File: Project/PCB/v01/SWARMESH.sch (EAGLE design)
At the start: 45 parts, among them IC1 4051N, M1 MOTOR10MM, M2 MOTOR10MM, Q1 TIP122, U1 ESP32DEVKITC, U3 L293D, U4 7805T

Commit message: added datasheets
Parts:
- removed C1: 10uF, adafruit:CPOL-USE10-20
- removed JBAT, JCHG: (no value), SparkFun-Connectors:M02-JST-2-PTH-NO_SILK
- removed LED1: TLLG4400, led:TLLG4400
- removed LED2: TLLR4400, led:TLLR4400
- removed LED3: TLLY4400, led:TLLY4400
- removed R1, R3: PHOTOCELLPTH, SparkFun-Sensors:PHOTOCELLPTH
- removed R10, R2, R4, R5, R6, R7: 1k, adafruit:R-US_0207/12
- removed R11, R8: 100, adafruit:R-US_0207/12
- removed R12, R9: 10k, adafruit:R-US_0207/12
- removed S1: (no value), SparkFun-Electromechanical:SWITCH-SPDTPTH2
- removed U$1, U$2: CNY70, cny70:CNY70
- removed U$3: PNA460XM, adafruit:PNA460XM
- removed U$4: PINHD-1X10, adafruit:PINHD-1X10
- added BAT+, BAT-, CHG1+, CHG1-, CHG2+, CHG2-: (no value), adafruit:PINHD-1X1-BIGPOGO
- added C5, C6: 10uF, adafruit:CPOL-USE2.5-7
- added JMUX: PINHD-1X10, adafruit:PINHD-1X10
- added RD1, RD2: 0, adafruit:R-US_0207/12
- added RS1, RS2: 150, adafruit:R-US_0207/12
- added S2: (no value), ArduinoNano LearningBot 4-21-18:SWITCH_320-938
- added T1, T2, T3, T4: (no value), SparkFun-Connectors:CONN_01SPRING-CONN
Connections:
- removed net N$22: R8.1, U$1.A
- removed net N$24: R1.P$1, R9.2
- removed net N$26: R10.2, U$2.COL
- removed net N$35: R12.2, R3.P$1
- new net ADO: JIMU.7
- new net E1A: JM1.3
- new net E1B: JM1.4
- new net E2A: JM2.3
- new net E2B: JM2.4
- new net ECL: JIMU.6
- new net EDA: JIMU.5
- new net FSY: JIMU.10
- new net INT: JIMU.8
- new net M1A: JM1.1, M1.+, U3.1Y
- new net M1B: JM1.6, M1.-, U3.2Y
- new net M2A: JM2.1, M2.-, U3.4Y
- new net M2B: JM2.6, M2.+, U3.3Y
- new net N$17: JMUX.10, RD1.2, RD2.1
- new net NCS: JIMU.9
- new net SCL: JI2C.5, JI2C.6, JIMU.3, U1.IO22
- new net SDA: JI2C.7, JI2C.8, JIMU.4, U1.IO21
- new net TOUCH1: T1.1, U1.IO15
- new net TOUCH2: T2.1, U1.IO2
- new net TOUCH3: T3.1, U1.IO0
- new net TOUCH4: T4.1, U1.IO4
- net GND: now also BAT-.1, C3.2, C5.-, C6.-, CHG1-.1, CHG2-.1, IC1A.INH, IC1P.GND, IC1P.VEE, JI2C.3, JI2C.4, JIMU.2, JM1.5, JM2.5, Q1.E, RD2.2; no longer C1.-, JBAT.2, JCHG.2, LED1.C, LED2.C, LED3.C, R1.P$2, R3.P$2, U$1.C, U$1.EMI, U$2.C, U$2.EMI, U$3.GND
- net N$1: now also Q1.B, R13.1; no longer LED1.A, R4.1
- net N$10: now also IC1A.X3, JMUX.4; no longer M1.+, U3.1Y
- net N$11: now also IC1A.X4, JMUX.5; no longer M1.-, U3.2Y
- net N$12: now also IC1A.X5, JMUX.6; no longer M2.-, U3.4Y
- net N$13: now also IC1A.X6, JMUX.7; no longer M2.+, U3.3Y
- net N$14: now also IC1A.X7, JMUX.8; no longer R4.2
- net N$15: now also C3.1, IC1A.X; no longer R5.2
- net N$16: now also C6.+, JMUX.9, RS1.1, RS2.1; no longer R6.2
- net N$18: now also IC1A.C; no longer R7.2, U$1.COL
- net N$19: now also IC1A.B; no longer R11.1, U$2.A
- net N$2: now also R13.2; no longer LED2.A, R5.1
- net N$20: now also IC1A.A; no longer U$3.OUT
- net N$21: now also BAT+.1, S21.P; no longer JCHG.1, S1.P
- net N$3: now also IC1A.X0, JMUX.1; no longer LED3.A, R6.1
- net N$37: now also RD1.1; no longer R2.1
- net N$8: now also IC1A.X1, JMUX.2; no longer U3.1-2EN
- net N$9: now also IC1A.X2, JMUX.3; no longer U3.3-4EN
- net V+: now also C5.+, CHG1+.1, CHG2+.1, RS2.2, S21.S; no longer C1.+, JBAT.1, S1.S
- net VCC: now also IC1P.VCC, JI2C.1, JI2C.2, JIMU.1, JM1.2, JM2.2, RS1.2, U3.1-2EN, U3.3-4EN; no longer R10.1, R11.2, R12.1, R7.1, R8.2, R9.1, U$3.VCC
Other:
- note added: "Select RS & RD to configure IR operation"
- note removed: "Remember to change battery footprint"
- note removed: "Remember to change switch footprint"
- moved on the sheet: C2, C3, IC1, JI2C, JM1, JM2, M1, Q1, R13, R14, R15, U1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

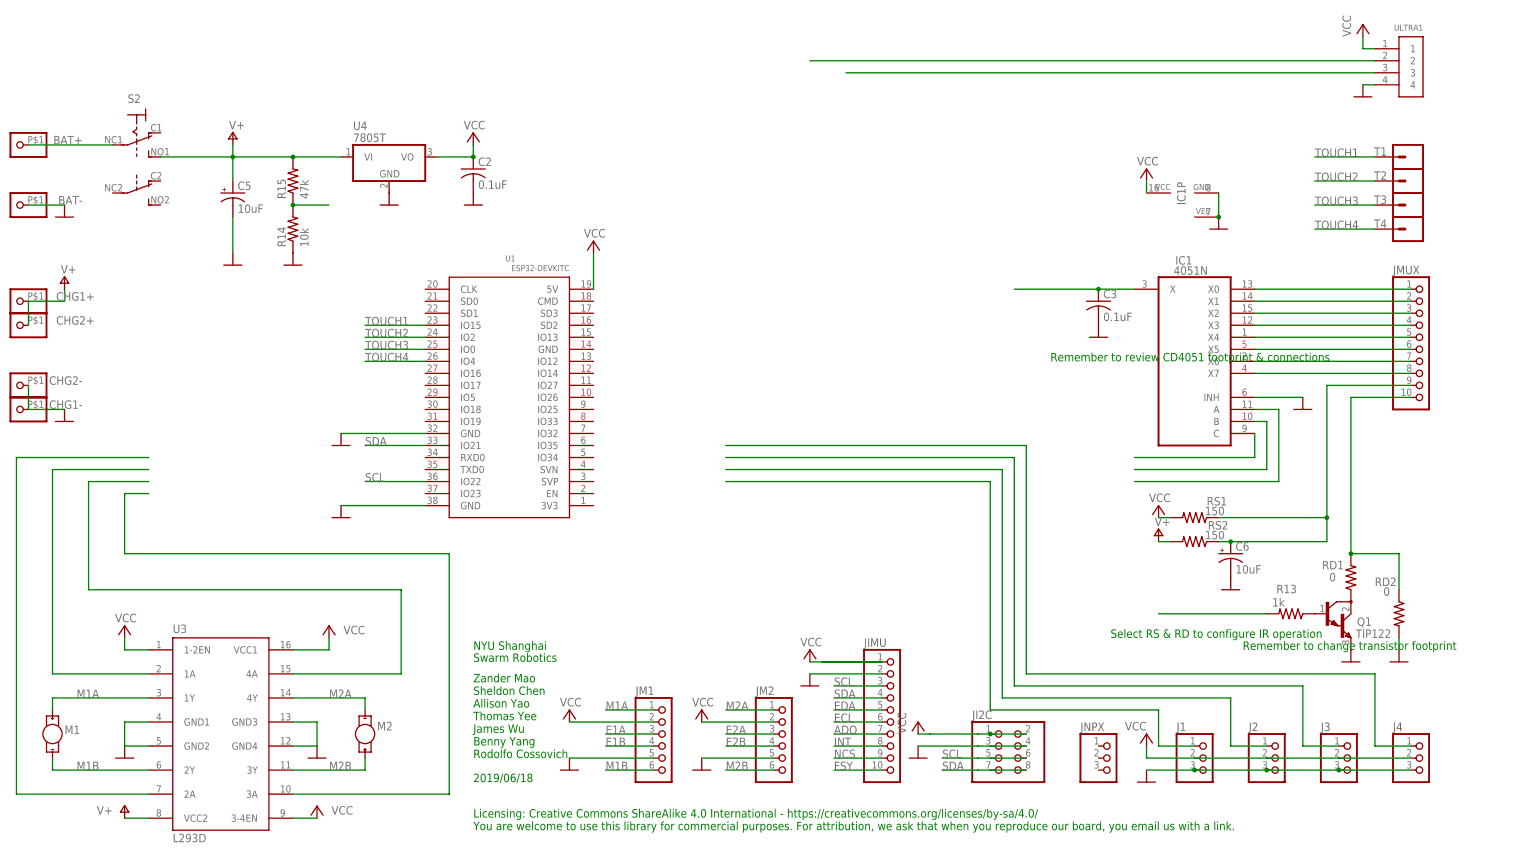
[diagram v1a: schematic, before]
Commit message: added CNY70 & touch sensors
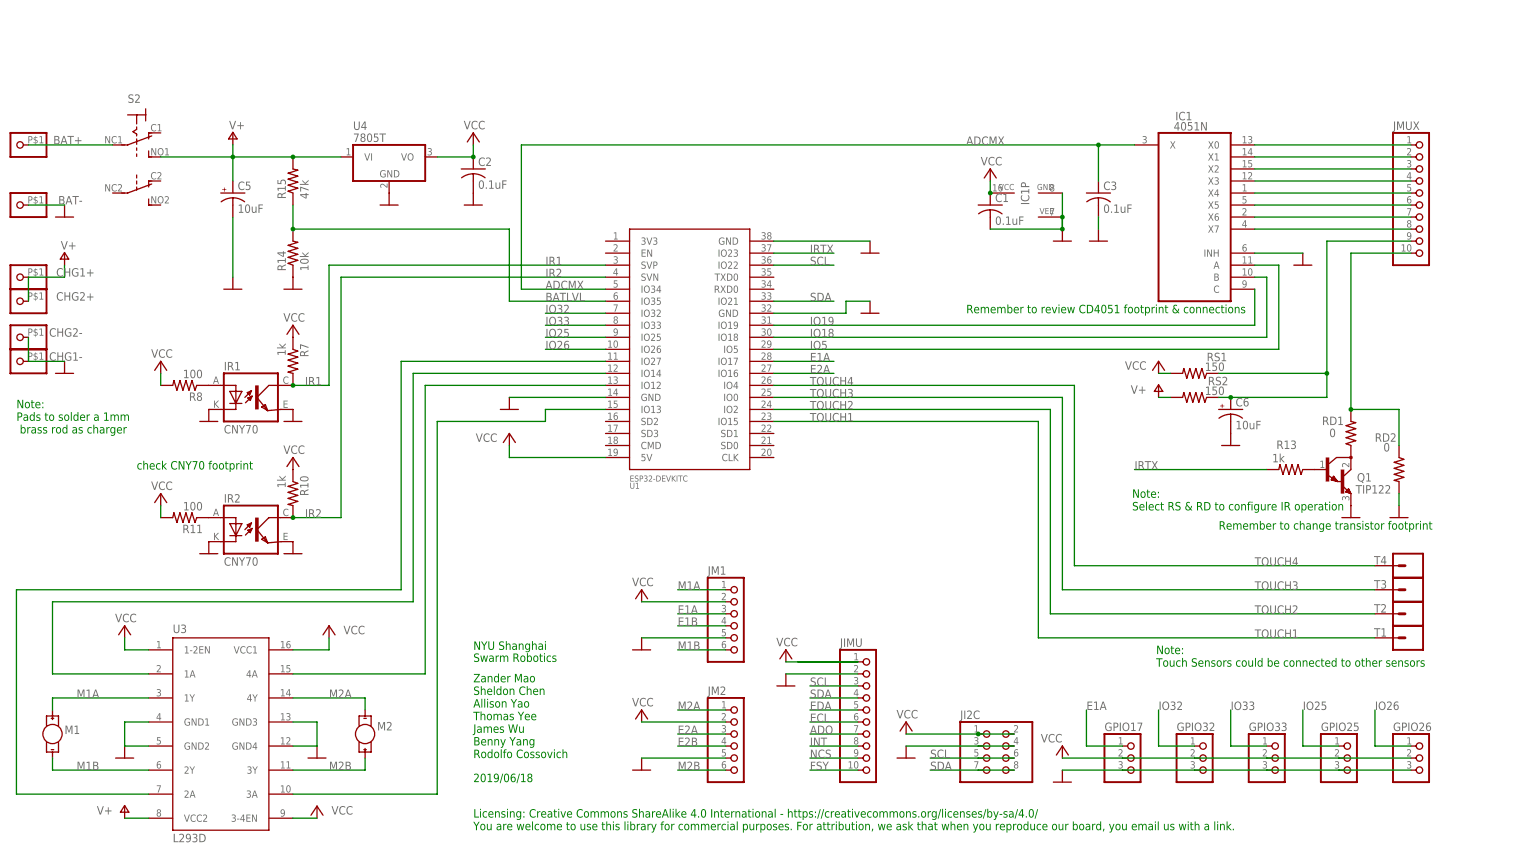
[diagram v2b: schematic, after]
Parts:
- removed JNPX: (no value), adafruit:PINHD-1X3
- removed ULTRA1: 1X4-BIG, adafruit:1X4-BIG
- added C1: 0.1uF, adafruit:C-US050-024X044
- added GPIO17: (no value), adafruit:PINHD-1X3
- added IR1, IR2: CNY70, cny70:CNY70
- added R10, R7: 1k, adafruit:R-US_0207/12
- added R11, R8: 100, adafruit:R-US_0207/12
- renumbered J1 to GPIO32, J2 to GPIO33, J3 to GPIO25, J4 to GPIO26
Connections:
- removed net N$15: C3.1, IC1A.X
- removed net N$18: IC1A.C
- removed net N$2: R13.2
- removed net N$20: IC1A.A
- removed net N$23: GPIO32.1
- removed net N$27: ULTRA1.2
- removed net N$28: ULTRA1.3
- removed net N$29: GPIO33.1
- removed net N$30: GPIO25.1
- removed net N$31: GPIO26.1
- removed net N$32: R14.2, R15.1
- removed net N$4: U3.1A
- removed net N$5: U3.2A
- removed net N$6: U3.4A
- removed net N$7: U3.3A
- new net ADCMX: C3.1, IC1A.X, U1.IO34
- new net BATLVL: R14.2, R15.1, U1.IO35
- new net IO18: IC1A.B, U1.IO18
- new net IO19: IC1A.C, U1.IO19
- new net IO25: GPIO25.1, U1.IO25
- new net IO26: GPIO26.1, U1.IO26
- new net IO32: GPIO32.1, U1.IO32
- new net IO33: GPIO33.1, U1.IO33
- new net IO5: IC1A.A, U1.IO12, U1.IO13, U1.IO14, U1.IO27, U1.IO5, U3.1A, U3.2A, U3.3A, U3.4A
- new net IR1: IR1.COL, R7.2, U1.SVP
- new net IR2: IR2.COL, R10.2, U1.SVN
- new net IRTX: R13.2, U1.IO23
- new net N$22: IR1.A, R8.1
- net E1A: now also GPIO17.1, U1.IO17
- net E2A: now also U1.IO16
- net GND: now also C1.2, GPIO17.3, IR1.C, IR1.EMI, IR2.C, IR2.EMI, U1.GND@14; no longer ULTRA1.4
- net N$19: now also IR2.A, R11.1; no longer IC1A.B
- net VCC: now also C1.1, GPIO17.2, R10.1, R11.2, R7.1, R8.2; no longer ULTRA1.1
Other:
- note added: "Note: Pads to solder a 1mm brass rod as charger"
- note added: "Note: Select RS & RD to configure IR operation"
- note added: "Note: Touch Sensors could be connected to other sensors"
- note added: "check CNY70 footprint"
- note removed: "Select RS & RD to configure IR operation"
- moved on the sheet: C3, C6, CHG1+, CHG1-, CHG2+, CHG2-, IC1, IC1P, JI2C, JIMU, JM1, JM2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

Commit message: first revision
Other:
- note added: "Licensing: Creative Commons ShareAlike 4.0 International - https://creativecommons.org/licenses/by-sa/4.0/ You are welcome to use this library for commercial purposes. For attribution, we ask that when you reproduce our board, you email us with a link. Acknowlewdgement: This project has been supported by NYU Shanghai Dean's Undergraduate Research Fund."
- note removed: "Licensing: Creative Commons ShareAlike 4.0 International - https://creativecommons.org/licenses/by-sa/4.0/ You are welcome to use this library for commercial purposes. For attribution, we ask that when you reproduce our board, you email us with a link."
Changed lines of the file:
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@@
 <text x="172.72" y="5.08" size="1.778" layer="91">
 Licensing: Creative Commons ShareAlike 4.0 International - https://creativecommons.org/licenses/by-sa/4.0/
-You are welcome to use this library for commercial purposes. For attribution, we ask that when you reproduce our board, you email us with a link.</text>
+You are welcome to use this library for commercial purposes. For attribution, we ask that when you reproduce our board, you email us with a link.
+Acknowlewdgement: This project has been supported by NYU Shanghai Dean's Undergraduate Research Fund.</text>
 <text x="276.86" y="114.3" size="1.778" layer="91">Remember to review CD4051 footprint &amp; connections</text>
 <text x="311.912" y="72.644" size="1.778" layer="91">Note:
